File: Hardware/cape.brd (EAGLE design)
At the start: 118.2 x 103.5 mm, 75 parts, among them IC1 RT7258, IC2 74VHC541, IC4 74VHC541, IC5 74VHC541, J1 FCI-10118064-5001310LF, J2 FCI-10118064-5001310LF, J3 RJ45-8P8C, J4 RJ45-8P8C, Q1 FDS6670, Q2 N-MOSFET-DUAL, Q3 N-MOSFET-DUAL, Q4 N-MOSFET-DUAL, Q5 N-MOSFET-DUAL, Q6 N-MOSFET-DUAL, Q7 N-MOSFET-DUAL, Q8 N-MOSFET-DUAL, Q9 N-MOSFET-DUAL

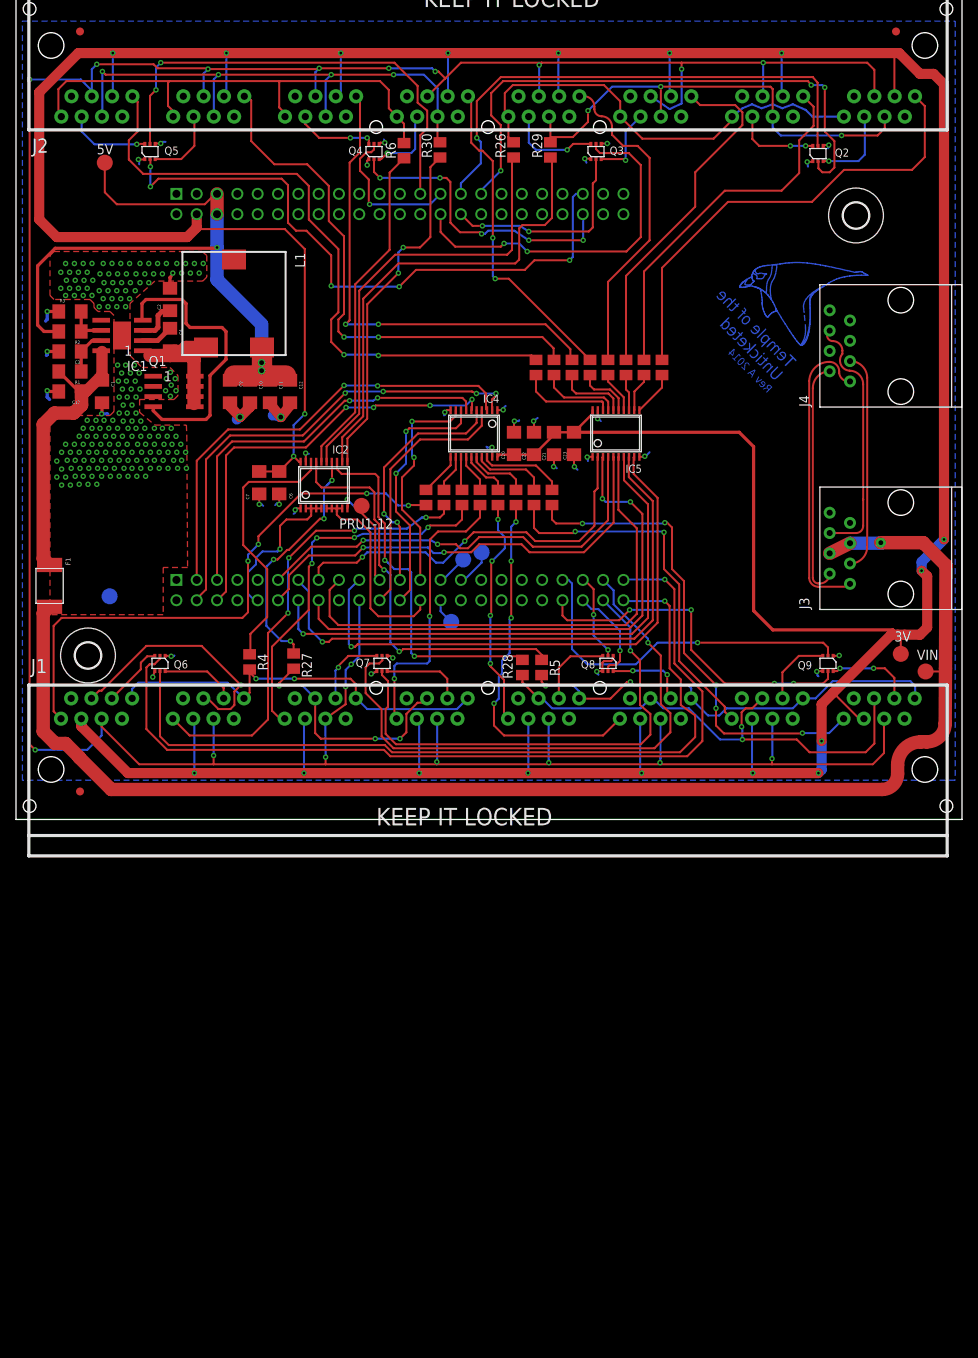
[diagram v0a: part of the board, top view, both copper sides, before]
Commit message: Added resistors (resolves #3), changed mosfet package (resolves #6), changed power input
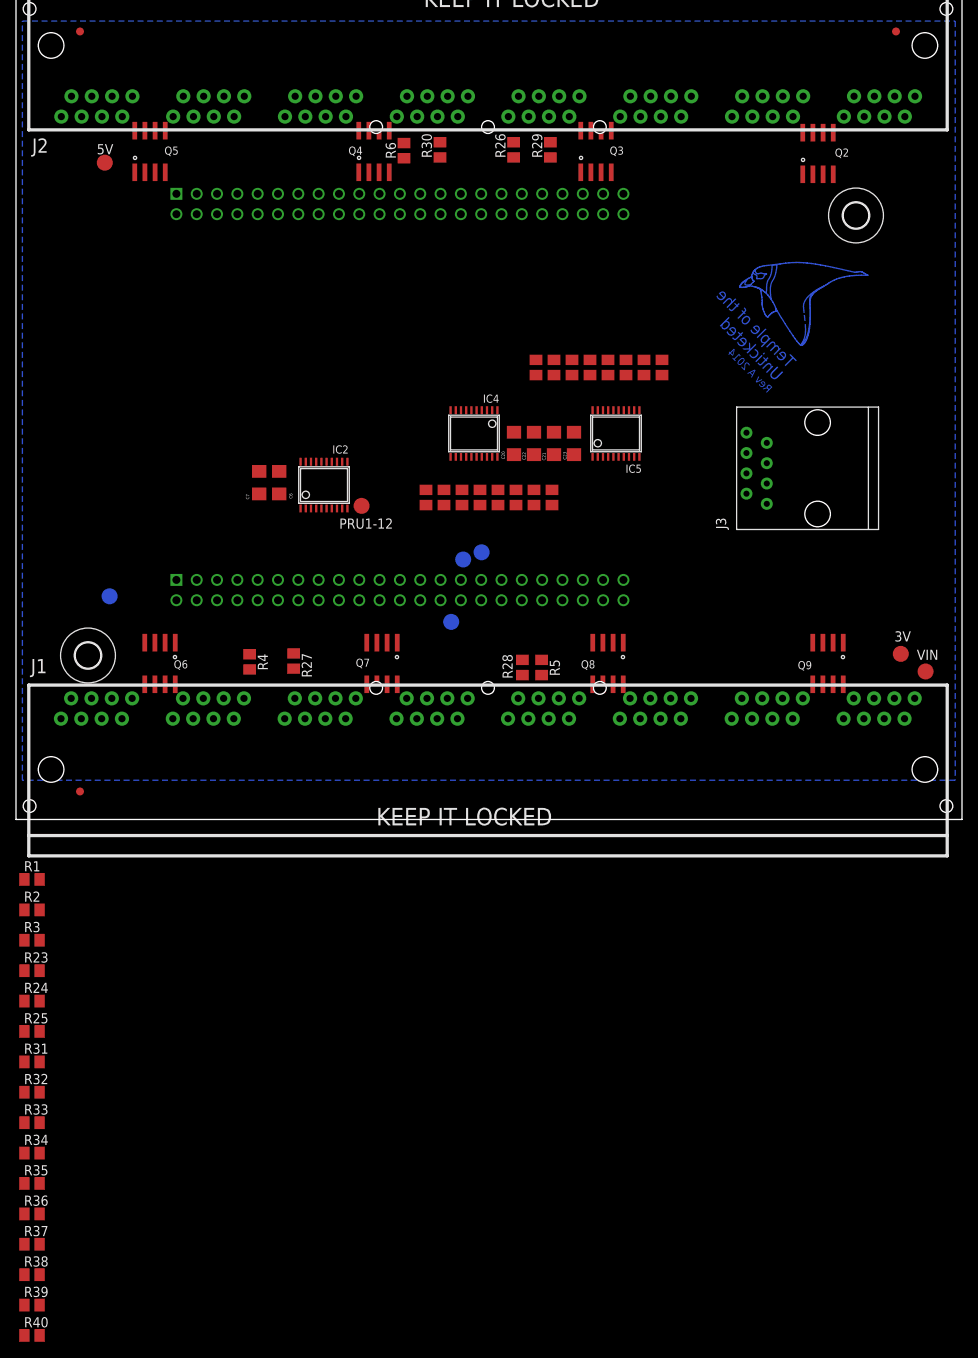
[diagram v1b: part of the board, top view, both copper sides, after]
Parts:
- removed C1, C10, C9: 22uF, SparkFun-Capacitors:1206
- removed C11, C12: 47uF, SparkFun-Capacitors:1206
- removed C17: 10uF, SparkFun-Capacitors:1206
- removed C2, C3, C4: 1uF, SparkFun-Capacitors:1206
- removed F1: PTC, cape:LF-1812L
- removed IC1: RT7258, TotU:SOP08-PAD
- removed J4: RJ45-8P8C, cape:54602-908LF
- removed L1: 2.8uH, TotU:MURATA_INDUCTOR_3900
- removed Q1: FDS6670, TotU:SOP08
- added R23, R24, R25, R31, R32, R33, R34, R35, R36, R37, R38, R39, R40: R18 1/2W, resistor:M0805
- Q2, Q3, Q4, Q5, Q6, Q7, Q8, Q9: value N-MOSFET-DUAL -> N-MOSFET-DUALSO8; device cape:TSSOP6 -> cape:SO8
- R1: value 100k -> R18 1/2W; device SparkFun-Passives:1206 -> resistor:M0805
- R2: value 93k -> R18 1/2W; device SparkFun-Passives:1206 -> resistor:M0805
- R3: value 18k -> R18 1/2W; device SparkFun-Passives:1206 -> resistor:M0805
- moved R3 78.7 mm to (2.00, -15.1)
- moved R2 72.5 mm to (2.00, -11.3), turned to 0 degrees
- moved R1 63.7 mm to (2.00, -7.50), turned to 0 degrees
- moved J3 14.4 mm to (100.2, 43.9)
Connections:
- removed net RX_N: J3.6, J4.6
- removed net RX_P: J3.3, J4.3
- removed net TX_N: J3.2, J4.2
- removed net TX_P: J3.1, J4.1
- removed net VFUSE: C1.1, C17.1, F1.P$1C, IC1.8, R1.2
- new net N$29: Q9.7, Q9.8, R31.2
- new net N$30: Q9.5, Q9.6, R32.2
- new net N$31: Q2.7, Q2.8, R33.2
- new net N$34: Q2.5, Q2.6, R34.2
- new net N$35: Q3.7, Q3.8, R35.2
- new net N$36: Q3.5, Q3.6, R36.2
- new net N$37: Q4.7, Q4.8, R37.2
- new net N$38: Q4.5, Q4.6, R38.2
- new net N$39: Q5.7, Q5.8, R39.2
- new net N$40: Q5.5, Q5.6, R40.2
- net BL0: now also R1.1; no longer Q6.3
- net BL1: now also R2.1; no longer Q6.6
- net BL10: now also R35.1; no longer Q3.3
- net BL11: now also R36.1; no longer Q3.6
- net BL12: now also R37.1; no longer Q4.3
- net BL13: now also R38.1; no longer Q4.6
- net BL14: now also R39.1; no longer Q5.3
- net BL15: now also R40.1; no longer Q5.6
- net BL2: now also R3.1; no longer Q7.3
- net BL3: now also R23.1; no longer Q7.6
- net BL4: now also R24.1; no longer Q8.3
- net BL5: now also R25.1; no longer Q8.6
- net BL6: now also R31.1; no longer Q9.3
- net BL7: now also R32.1; no longer Q9.6
- net BL8: now also R33.1; no longer Q2.3
- net BL9: now also R34.1; no longer Q2.6
- net GND: now also J3.1, J3.3, J3.5, Q2.3, Q3.3, Q4.3, Q5.3, Q6.3, Q7.3, Q8.3, Q9.3; no longer C1.2, C10.2, C11.2, C12.2, C17.2, C2.2, C3.2, C9.2, IC1.5, IC1.EXP, J3.8, Q1.1, Q1.2, Q1.3, Q2.4, Q3.4, Q4.4, Q5.4, Q6.4, Q7.4, Q8.4, Q9.4, R3.1
- net N$1: now also Q6.7, Q6.8, R1.2; no longer C2.1, IC1.3
- net N$2: now also Q6.5, Q6.6, R2.2; no longer C3.1, IC1.7, R1.1
- net N$3: now also Q7.7, Q7.8, R3.2; no longer C4.1, IC1.2
- net N$4: now also Q7.5, Q7.6, R23.2; no longer C4.2, IC1.1, L1.1, Q1.5, Q1.6, Q1.7, Q1.8
- net N$7: now also Q8.7, Q8.8, R24.2; no longer IC1.6, R2.1, R3.2
- net N$8: now also Q8.5, Q8.6, R25.2; no longer IC1.4, Q1.4
- net PRU0-1: now also Q2.4; no longer Q2.5
- net PRU0-3: now also Q3.4; no longer Q3.5
- net PRU0-5: now also Q4.4; no longer Q4.5
- net PRU0-7: now also Q5.4; no longer Q5.5
- net PRU1-1: now also Q6.4; no longer Q6.5
- net PRU1-3: now also Q7.4; no longer Q7.5
- net PRU1-5: now also Q8.4; no longer Q8.5
- net PRU1-7: now also Q9.4; no longer Q9.5
- net VCC5V: now also J3.2, J3.4, J3.6, J3.8; no longer C10.1, C11.1, C12.1, C9.1, L1.2, R2.2
- net VIN: no longer F1.P$2, J3.4, J3.5
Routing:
- net VCC3V3: track 564.1 -> 0.00 mm, vias 19 -> 0
- net RST: track 396.5 -> 0.00 mm, vias 18 -> 0
- net VIN: track 174.4 -> 0.00 mm, vias 1 -> 0
- net PRU1-0: track 109.2 -> 0.00 mm, vias 1 -> 0
- net PRU1-1: track 100.6 -> 0.00 mm, vias 1 -> 0
- net VCC5V: track 94.2 -> 0.00 mm, vias 3 -> 0
- net DATA15: track 80.4 -> 0.00 mm, vias 2 -> 0
- net PRU0-6: track 77.7 -> 0.00 mm, vias 5 -> 0
- net AD9: track 73.1 -> 0.00 mm, vias 1 -> 0
- net PRU1-2: track 72.7 -> 0.00 mm, vias 1 -> 0
- net DATA0: track 71.3 -> 0.00 mm, vias 4 -> 0
- net PRU0-0: track 70.7 -> 0.00 mm, vias 3 -> 0
- net AD8: track 70.6 -> 0.00 mm, vias 1 -> 0
- net GND: track 70.4 -> 0.00 mm, vias 231 -> 0
- net AD10: track 69.8 -> 0.00 mm, vias 1 -> 0
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- removed copper zone on layer 1, net GND

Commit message: Started adding A/B switches and more ports
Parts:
- removed R1, R2, R23, R24, R25, R3, R31, R32, R33, R34, R35, R36, R37, R38, R39, R40: R18 1/2W, resistor:M0805
- removed R10, R11, R12, R13, R14, R15, R16, R17, R18, R19, R20, R21, R22, R26, R27, R28, R29, R30, R4, R5, R6, R7, R8, R9: (no value), resistor:M0805
- added C1, C4: 10uF, SparkFun-Capacitors:1206
- added C2, C3: 1uF, SparkFun-Capacitors:1206
- added U$7, U$8: SN74CBT16292DLRSSOP56, cape:SSOP56
- moved IC5 34.7 mm to (41.7, 38.5)
- moved C6 29.3 mm to (49.3, 66.4)
- moved IC4 27.1 mm to (31.9, 38.5), turned to 0 degrees
- moved C7 25.9 mm to (42.6, 64.9)
- moved PRU1-12 25.0 mm to (63.2, 24.2)
- moved IC2 14.6 mm to (52.7, 38.6)
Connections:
- removed net N$10: IC2.17, R5.1
- removed net N$11: IC2.16, R6.1
- removed net N$12: IC2.15, R26.1
- removed net N$13: IC4.16, R9.1
- removed net N$14: IC2.14, R27.1
- removed net N$15: IC2.13, R28.1
- removed net N$16: IC4.15, R10.1
- removed net N$17: IC4.14, R11.1
- removed net N$18: IC4.13, R12.1
- removed net N$19: IC4.12, R13.1
- removed net N$20: IC4.11, R14.1
- removed net N$21: IC5.18, R15.1
- removed net N$22: IC5.17, R16.1
- removed net N$23: IC5.16, R17.1
- removed net N$24: IC5.15, R18.1
- removed net N$25: IC5.14, R19.1
- removed net N$26: IC5.13, R20.1
- removed net N$27: IC5.12, R21.1
- removed net N$28: IC5.11, R22.1
- removed net N$32: IC2.12, R29.1
- removed net N$33: IC2.11, R30.1
- removed net N$5: IC4.18, R7.1
- removed net N$6: IC4.17, R8.1
- removed net N$9: IC2.18, R4.1
- new net 10A: IC5.17, U$7.23
- new net 11A: IC5.16, U$7.25
- new net 12A: IC5.15, U$7.27
- new net 13A: IC5.14, U$8.2
- new net 14A: IC5.13, U$8.4
- new net 15A: IC5.12, U$8.6
- new net 16A: IC5.11, U$8.9
- new net 17A: IC2.15, U$8.11, U$8.13
- new net 19A: IC2.14, U$8.15, U$8.18
- new net 1A: IC4.18, U$7.2
- new net 21A: IC2.13, U$8.21, U$8.23
- new net 23A: IC2.12, U$8.25, U$8.27
- new net 2A: IC4.17, U$7.4
- new net 3A: IC4.16, U$7.6
- new net 4A: IC4.15, U$7.9
- new net 5A: IC4.14, U$7.11
- new net 6A: IC4.13, U$7.13
- new net 7A: IC4.12, U$7.15
- new net 8A: IC4.11, U$7.18
- new net 9A: IC5.18, U$7.21
- new net SCL_1: IC2.18, IC2.3, IC2.4
- new net SCL_2: IC2.17, IC2.5, IC2.6
- new net SCL_3: IC2.16, IC2.7, IC2.8
- net AD0: now also IC5.9; no longer IC4.9
- net AD1: now also IC5.8; no longer IC4.8
- net AD10: now also IC4.9; no longer IC5.7
- net AD11: now also IC5.4; no longer IC5.6
- net AD12: now also IC4.7; no longer IC5.5
- net AD13: now also IC4.6; no longer IC5.4
- net AD2: now also IC4.4; no longer IC4.7
- net AD3: now also IC4.5; no longer IC4.6
- net AD4: now also IC5.7; no longer IC4.5
- net AD5: now also IC5.6; no longer IC4.4
- net AD6: now also IC4.2; no longer IC4.3
- net AD7: now also IC4.3; no longer IC4.2
- net AD8: now also IC5.5; no longer IC5.9
- net AD9: now also IC4.8; no longer IC5.8
- net BL0: no longer R1.1
- net BL1: no longer R2.1
- net BL10: no longer R35.1
- net BL11: no longer R36.1
- net BL12: no longer R37.1
- net BL13: no longer R38.1
- net BL14: no longer R39.1
- net BL15: no longer R40.1
- net BL2: no longer R3.1
- net BL3: no longer R23.1
- net BL4: no longer R24.1
- net BL5: no longer R25.1
- net BL6: no longer R31.1
- net BL7: no longer R32.1
- net BL8: no longer R33.1
- net BL9: no longer R34.1
- net DATA0: no longer R14.2
- net DATA1: no longer R13.2
- net DATA10: no longer R20.2
- net DATA11: no longer R19.2
- net DATA12: no longer R18.2
- net DATA13: no longer R17.2
- net DATA14: no longer R16.2
- net DATA15: no longer R15.2
- net DATA2: no longer R12.2
- net DATA3: no longer R11.2
- net DATA4: no longer R10.2
- net DATA5: no longer R9.2
- net DATA6: no longer R8.2
- net DATA7: no longer R7.2
- net DATA8: no longer R22.2
- net DATA9: no longer R21.2
- net DC0: no longer R27.2
- net DC1: no longer R28.2
- net DC2: no longer R29.2
- net DC3: no longer R30.2
- net DC_RAW: no longer IC2.6, IC2.7, IC2.8, IC2.9
- net GND: now also C1.2, C2.2, C3.2, C4.2, U$7.19, U$7.38, U$7.49, U$7.8, U$8.19, U$8.38, U$8.49, U$8.8
- net N$1: no longer R1.2
- net N$2: no longer R2.2
- net N$29: no longer R31.2
- net N$3: no longer R3.2
- net N$30: no longer R32.2
- net N$31: no longer R33.2
- net N$34: no longer R34.2
- net N$35: no longer R35.2
- net N$36: no longer R36.2
- net N$37: no longer R37.2
- net N$38: no longer R38.2
- net N$39: no longer R39.2
- net N$4: no longer R23.2
- net N$40: no longer R40.2
- net N$7: no longer R24.2
- net N$8: no longer R25.2
- net SCK0: no longer R4.2
- net SCK1: no longer R5.2
- net SCK2: no longer R26.2
- net SCK3: no longer R6.2
- net SCL_RAW: no longer IC2.3, IC2.4, IC2.5
- net VCC5V: now also C1.1, C2.1, C3.1, C4.1, U$7.17, U$8.17
